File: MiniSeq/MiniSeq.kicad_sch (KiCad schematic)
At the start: 70 parts

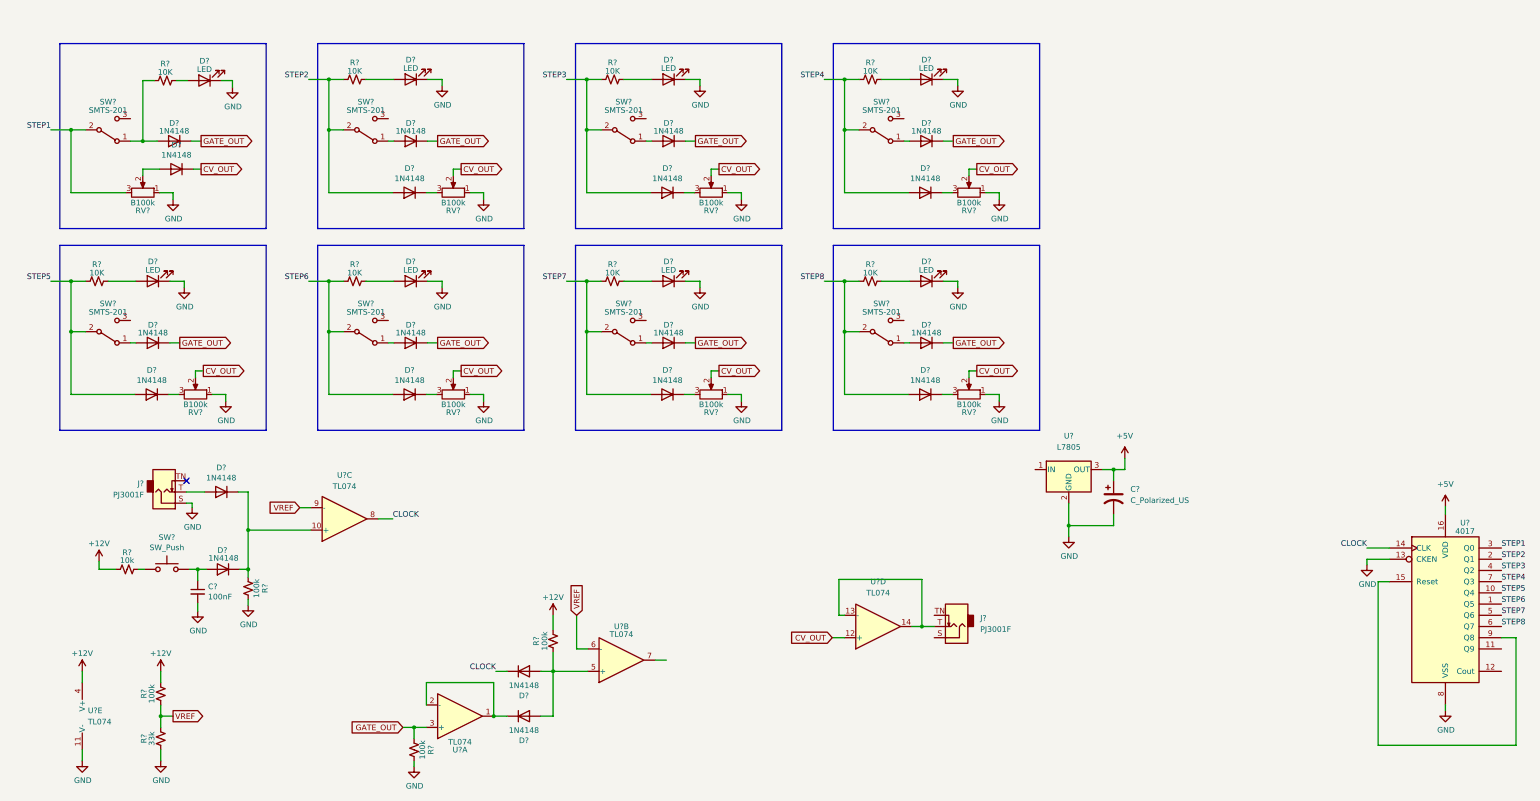
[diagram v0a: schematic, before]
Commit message: Fixed schematic layout
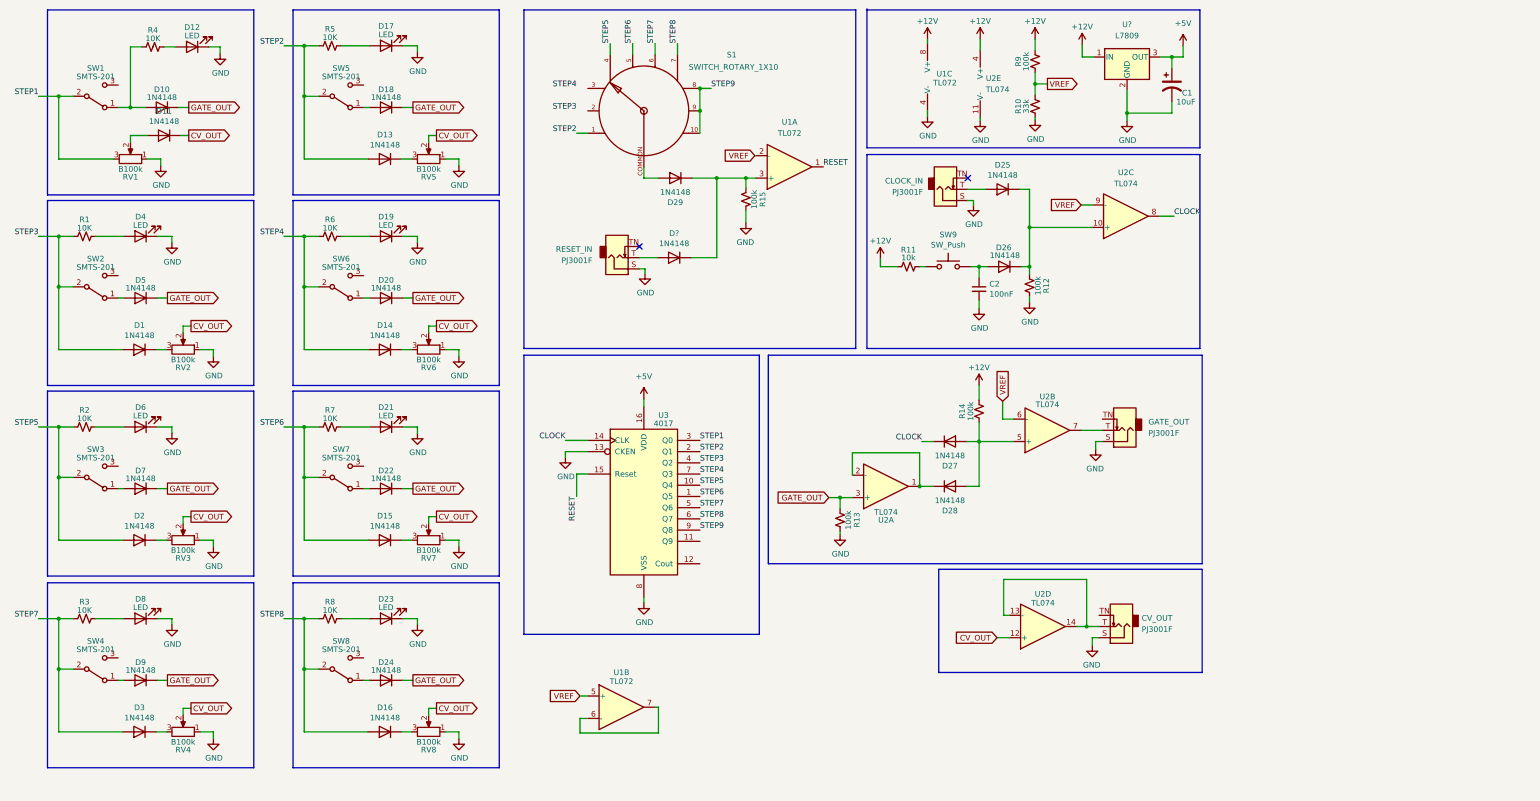
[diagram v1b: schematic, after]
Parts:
- removed U?: L7805, symbol Regulator_Linear:L7805
- added D29, D?: 1N4148, Diode_THT:D_DO-35_SOD27_P7.62mm_Horizontal, symbol Diode:1N4148
- added GATE_OUT, RESET_IN: PJ3001F, symbol benjiaomodular:PJ3001F
- added R15: 100k, symbol Device:R_Small_US
- added S1: SWITCH_ROTARY_1X10, ROTARY_SWITCH_1X10, symbol Sparkfun Electro Mechanical:SWITCH_ROTARY_1X10
- added U1: TL072, symbol Amplifier_Operational:TL072
- added U?: L7809, symbol Regulator_Linear:L7809
- C1: renamed from C?; value C_Polarized_US -> 10uF
- gave numbers to parts that had none: 64
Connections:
- net +12V: now also U1.8 (V+), U?.1 (IN)
- net +5V: now also U?.3 (OUT)
- net GND: now also CV_OUT.S, GATE_OUT.S, R15.2, RESET_IN.S, U1.4 (V-), U?.2 (GND)
- net STEP2: now also S1.1
- net STEP5: now also S1.4
- net STEP6: now also S1.5
- net STEP7: now also S1.6
- net STEP8: now also S1.7
- net VREF: now also U1.2 (-), U1.5 (+)
- net at U2.7: now also GATE_OUT.T
- net RESET: now reaches U3.15 (Reset)
- net RESET: now also U1.1; no longer U3.9 (Q8)
- new net: D29.1 (K), D?.1 (K), R15.1, U1.3 (+)
- new net: D29.2 (A), S1.COMMON
- new net: D?.2 (A), RESET_IN.T
- new net STEP9: S1.10, S1.8, S1.9, U3.9 (Q8)
- no-connect marks 1 -> 2
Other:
- company: (none) -> benjiaomodular
- title: (none) -> MiniSeq
- moved on the sheet: C1, C2, CLOCK_IN, CV_OUT, D1, D10, D11, D12, D13, D14, D15, D16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

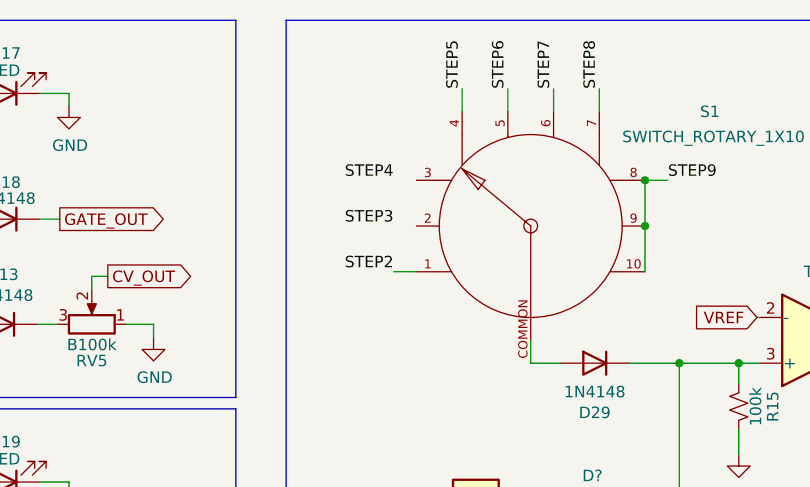
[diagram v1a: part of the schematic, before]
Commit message: Added some docs + schematics
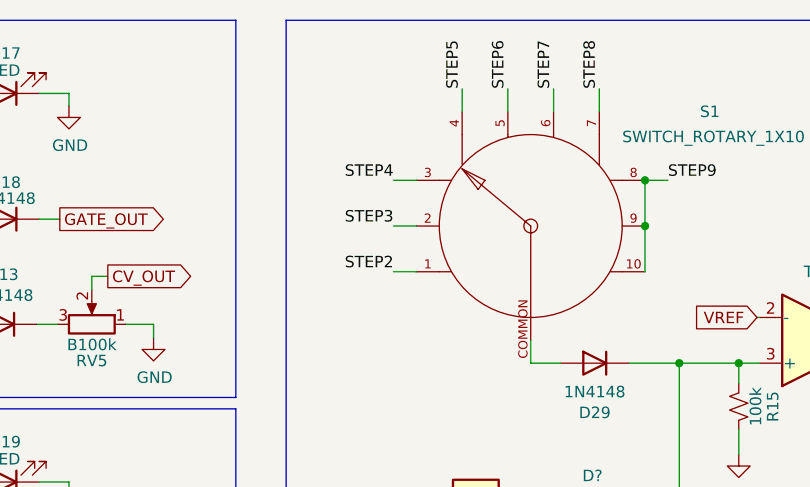
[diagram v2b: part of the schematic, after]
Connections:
- net STEP3: now also S1.2
- net STEP4: now also S1.3
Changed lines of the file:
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@@
+    (stroke (width 0) (type default) (color 0 0 0 0))
+  )
+  (wire (pts (xy 142.494 33.02) (xy 145.034 33.02))
     (stroke (width 0) (type default) (color 0 0 0 0))
   )
@@
     (stroke (width 0) (type default) (color 0 0 0 0))
   )
+  (wire (pts (xy 142.494 38.1) (xy 145.034 38.1))
+    (stroke (width 0) (type default) (color 0 0 0 0))
+  )
